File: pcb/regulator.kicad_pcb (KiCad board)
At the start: 2 copper layers, 60 x 68 mm, 28 parts, among them J1 Conn_01x06, U1 TL082

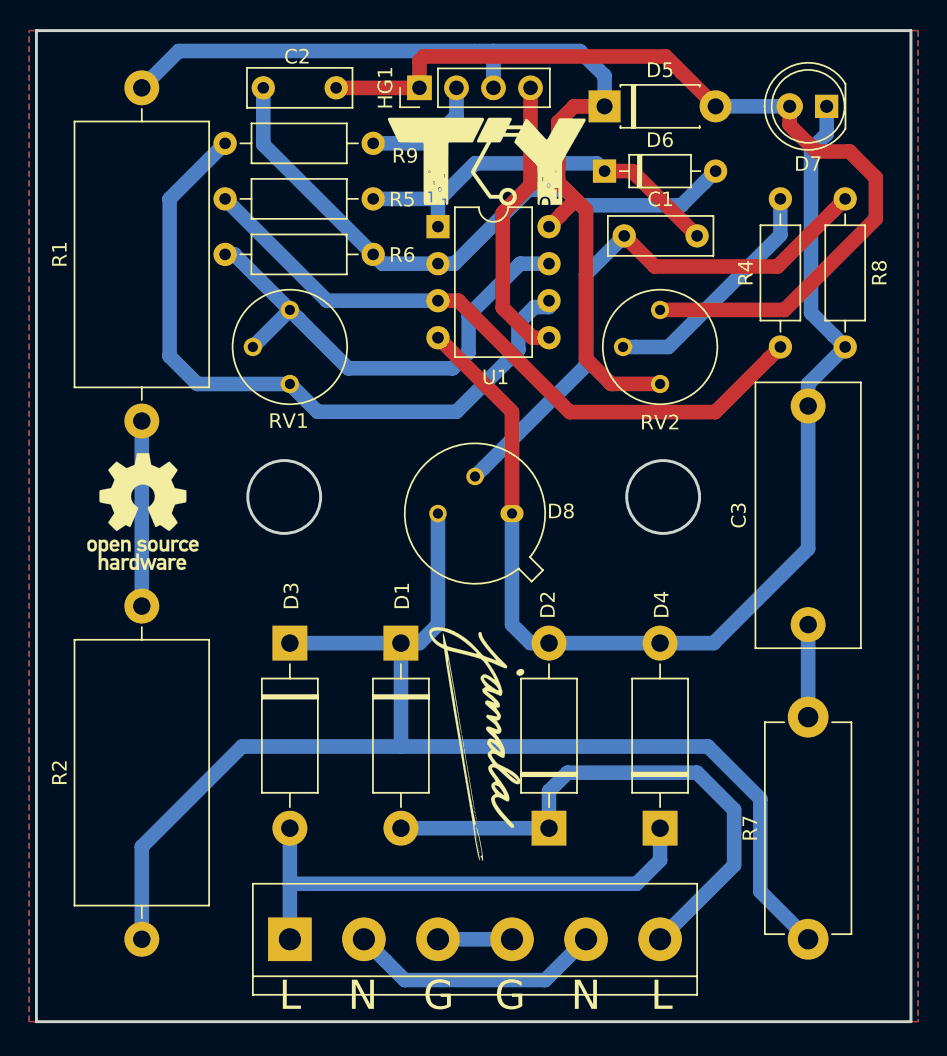
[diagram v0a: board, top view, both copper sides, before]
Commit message: Update QR code, exchange of mounting hole (add vias to outline)
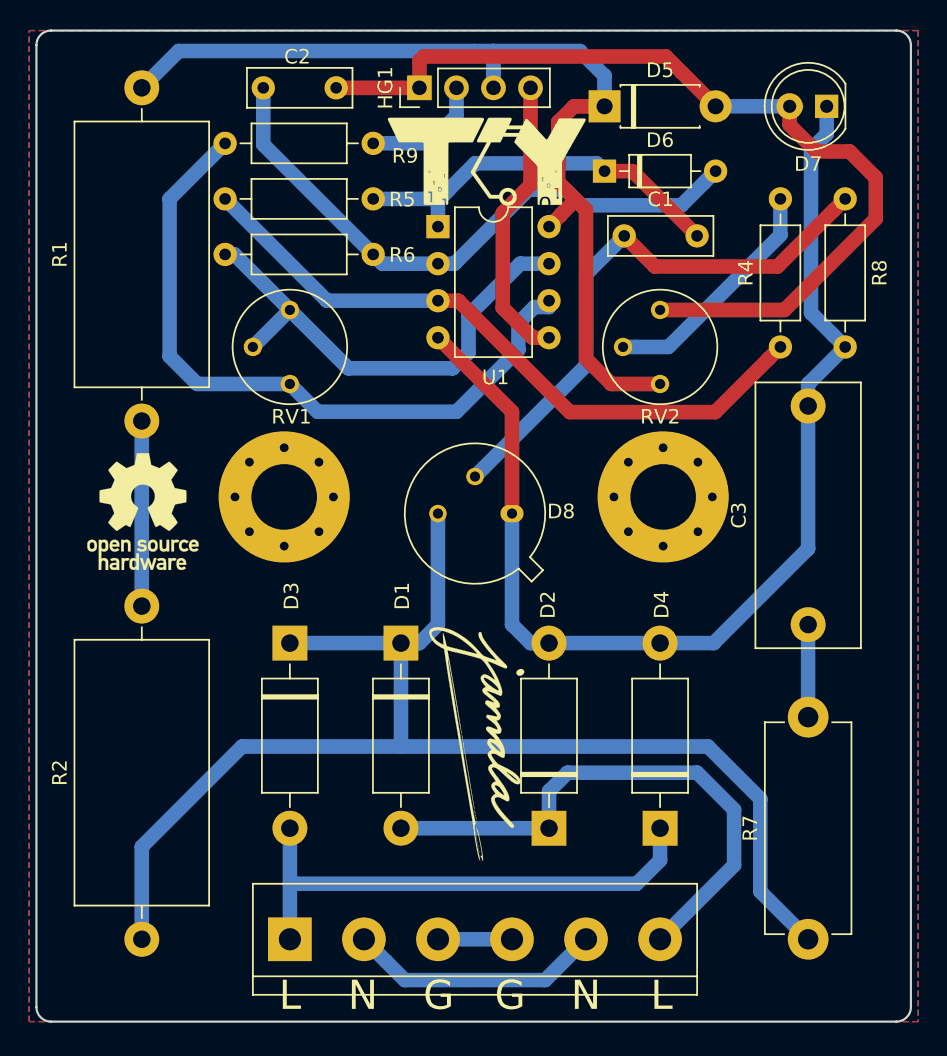
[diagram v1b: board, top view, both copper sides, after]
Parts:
- added REF**: MountingHole_4.5mm_Pad_Via, MountingHole:MountingHole_4.5mm_Pad_Via, F.Cu at (161.5, 103.0)
- added REF**: MountingHole_4.5mm_Pad_Via, MountingHole:MountingHole_4.5mm_Pad_Via, F.Cu at (135.5, 103.0)
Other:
- outline, holes or cut-outs redrawn
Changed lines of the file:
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@@
     (tracks 149)
     (zones 0)
-    (modules 28)
+    (modules 30)
     (nets 20)
   )
@@
     (visible_elements FFFFFF7F)
     (pcbplotparams
-      (layerselection 0x00000_ffffffff)
-      (usegerberextensions false)
+      (layerselection 0x010f0_ffffffff)
+      (usegerberextensions true)
       (usegerberattributes false)
       (usegerberadvancedattributes false)
@@
       (padsonsilk false)
       (subtractmaskfromsilk false)
-      (outputformat 4)
+      (outputformat 1)
       (mirror false)
-      (drillshape 2)
+      (drillshape 0)
       (scaleselection 1)
-      (outputdirectory ""))
+      (outputdirectory "gerber/"))
   )
   (net 0 "")
@@
     (descr "Potentiometer, vertical, Bourns 3339P, http://www.bourns.com/docs/Product-Datasheets/3339.pdf")
     (tags "Potentiometer vertical Bourns 3339P")
-    (fp_text reference RV1 (at -0.09 2.55) (layer F.SilkS)
+    (fp_text reference RV1 (at 0.11 2.25) (layer F.SilkS)
       (effects (font (size 1 1) (thickness 0.15)))
     )
@@
     (descr "Potentiometer, vertical, Bourns 3339P, http://www.bourns.com/docs/Product-Datasheets/3339.pdf")
     (tags "Potentiometer vertical Bourns 3339P")
-    (fp_text reference RV2 (at 0.01 2.65) (layer F.SilkS)
+    (fp_text reference RV2 (at 0.01 2.25) (layer F.SilkS)
       (effects (font (size 1 1) (thickness 0.15)))
     )
@@
       (xy 5.73024 -5.73024)) (layer B.SilkS) (width 0.01))
   )
+  (module MountingHole:MountingHole_4.5mm_Pad_Via (layer F.Cu)
+    (at 161.5 103)
+    (descr "Mounting Hole 4.5mm")
+    (tags "mounting hole 4.5mm")
+    (attr virtual)
+    (fp_text reference REF** (at 0 -5.5) (layer F.SilkS) hide
+      (effects (font (size 1 1) (thickness 0.15)))
+    )
+    (fp_text value MountingHole_4.5mm_Pad_Via (at 0 5.5) (layer F.Fab)
+      (effects (font (size 1 1) (thickness 0.15)))
+    )
+    (fp_circle (center 0 0) (end 4.75 0) (layer F.CrtYd) (width 0.05))
+    (fp_circle (center 0 0) (end 4.5 0) (layer Cmts.User) (width 0.15))
+    (fp_text user %R (at 0.3 0) (layer F.Fab)
+      (effects (font (size 1 1) (thickness 0.15)))
+    )
+    (pad 1 thru_hole circle (at 2.386485 -2.386485) (size 0.9 0.9) (drill 0.6) (layers *.Cu *.Mask))
+    (pad 1 thru_hole circle (at 0 -3.375) (size 0.9 0.9) (drill 0.6) (layers *.Cu *.Mask))
+    (pad 1 thru_hole circle (at -2.386485 -2.386485) (size 0.9 0.9) (drill 0.6) (layers *.Cu *.Mask))
+    (pad 1 thru_hole circle (at -3.375 0) (size 0.9 0.9) (drill 0.6) (layers *.Cu *.Mask))
+    (pad 1 thru_hole circle (at -2.386485 2.386485) (size 0.9 0.9) (drill 0.6) (layers *.Cu *.Mask))
+    (pad 1 thru_hole circle (at 0 3.375) (size 0.9 0.9) (drill 0.6) (layers *.Cu *.Mask))
+    (pad 1 thru_hole circle (at 2.386485 2.386485) (size 0.9 0.9) (drill 0.6) (layers *.Cu *.Mask))
+    (pad 1 thru_hole circle (at 3.375 0) (size 0.9 0.9) (drill 0.6) (layers *.Cu *.Mask))
+    (pad 1 thru_hole circle (at 0 0) (size 9 9) (drill 4.5) (layers *.Cu *.Mask))
+  )
+  (module MountingHole:MountingHole_4.5mm_Pad_Via (layer F.Cu)
+    (at 135.5 103)
+    (descr "Mounting Hole 4.5mm")
+    (tags "mounting hole 4.5mm")
+    (attr virtual)
+    (fp_text reference REF** (at 0 -5.5) (layer F.SilkS) hide
+      (effects (font (size 1 1) (thickness 0.15)))
+    )
+    (fp_text value MountingHole_4.5mm_Pad_Via (at 0 5.5) (layer F.Fab)
+      (effects (font (size 1 1) (thickness 0.15)))
+    )
+    (fp_circle (center 0 0) (end 4.75 0) (layer F.CrtYd) (width 0.05))
+    (fp_circle (center 0 0) (end 4.5 0) (layer Cmts.User) (width 0.15))
+    (fp_text user %R (at 0.3 0) (layer F.Fab)
+      (effects (font (size 1 1) (thickness 0.15)))
+    )
+    (pad 1 thru_hole circle (at 2.386485 -2.386485) (size 0.9 0.9) (drill 0.6) (layers *.Cu *.Mask))
+    (pad 1 thru_hole circle (at 0 -3.375) (size 0.9 0.9) (drill 0.6) (layers *.Cu *.Mask))
+    (pad 1 thru_hole circle (at -2.386485 -2.386485) (size 0.9 0.9) (drill 0.6) (layers *.Cu *.Mask))
+    (pad 1 thru_hole circle (at -3.375 0) (size 0.9 0.9) (drill 0.6) (layers *.Cu *.Mask))
+    (pad 1 thru_hole circle (at -2.386485 2.386485) (size 0.9 0.9) (drill 0.6) (layers *.Cu *.Mask))
+    (pad 1 thru_hole circle (at 0 3.375) (size 0.9 0.9) (drill 0.6) (layers *.Cu *.Mask))
+    (pad 1 thru_hole circle (at 2.386485 2.386485) (size 0.9 0.9) (drill 0.6) (layers *.Cu *.Mask))
+    (pad 1 thru_hole circle (at 3.375 0) (size 0.9 0.9) (drill 0.6) (layers *.Cu *.Mask))
+    (pad 1 thru_hole circle (at 0 0) (size 9 9) (drill 4.5) (layers *.Cu *.Mask))
+  )
+  (gr_line (start 177.5 139) (end 119.5 139) (layer Edge.Cuts) (width 0.15))
+  (gr_arc (start 177.5 138) (end 177.5 139) (angle -90) (layer Edge.Cuts) (width 0.15))
+  (gr_arc (start 119.5 138) (end 118.5 138) (angle -90) (layer Edge.Cuts) (width 0.15))
+  (gr_line (start 118.5 72) (end 118.5 138) (layer Edge.Cuts) (width 0.15))
+  (gr_line (start 178.5 72) (end 178.5 138) (layer Edge.Cuts) (width 0.15))
+  (gr_line (start 119.5 71) (end 177.5 71) (layer Edge.Cuts) (width 0.15))
+  (gr_arc (start 119.5 72) (end 119.5 71) (angle -90) (layer Edge.Cuts) (width 0.15))
+  (gr_arc (start 177.5 72) (end 178.5 72) (angle -90) (layer Edge.Cuts) (width 0.15))
   (gr_text L (at 161.4 137.2) (layer F.SilkS)
     (effects (font (size 2 2) (thickness 0.4)))
@@
   )
   (gr_line (start 148.59 70.485) (end 148.59 67.945) (layer Cmts.User) (width 0.2))
-  (gr_circle (center 135.5 103.08) (end 130.48 102.65) (layer Cmts.User) (width 0.2))
-  (gr_circle (center 161.49 103.08) (end 156.47 102.71) (layer Cmts.User) (width 0.2))
-  (gr_circle (center 135.5011 103.0036) (end 138.0011 103.0036) (layer Edge.Cuts) (width 0.2))
-  (gr_line (start 178.5011 71.0036) (end 118.5011 71.0036) (layer Edge.Cuts) (width 0.2))
-  (gr_line (start 178.5011 71.0036) (end 178.5011 139.0036) (layer Edge.Cuts) (width 0.2))
-  (gr_circle (center 161.5011 103.0036) (end 164.0011 103.0036) (layer Edge.Cuts) (width 0.2))
-  (gr_line (start 118.5011 71.0036) (end 118.5011 139.0036) (layer Edge.Cuts) (width 0.2))
-  (gr_line (start 178.5011 139.0036) (end 118.5011 139.0036) (layer Edge.Cuts) (width 0.2))
   (segment (start 149.189999 101.000001) (end 148.59 101.6) (width 1) (layer B.Cu) (net 1) (status 30))
   (segment (start 158.83 85.09) (end 156.21 87.71) (width 1) (layer B.Cu) (net 1) (status 10))
@@
   (segment (start 129.54 95.25) (end 135.89 95.25) (width 1) (layer B.Cu) (net 18) (status 20))
   (segment (start 127.635 93.345) (end 129.54 95.25) (width 1) (layer B.Cu) (net 18))
+  (segment (start 152.661999 89.974999) (end 153.67 89.974999) (width 1) (layer B.Cu) (net 18) (status 20))
+  (segment (start 151.569999 91.066999) (end 152.661999 89.974999) (width 1) (layer B.Cu) (net 18))
+  (segment (start 151.569999 92.905001) (end 151.569999 91.066999) (width 1) (layer B.Cu) (net 18))
+  (segment (start 147.32 97.155) (end 151.569999 92.905001) (width 1) (layer B.Cu) (net 18))
+  (segment (start 135.89 95.25) (end 137.795 97.155) (width 1) (layer B.Cu) (net 18) (status 10))
+  (segment (start 137.795 97.155) (end 147.32 97.155) (width 1) (layer B.Cu) (net 18))
   (segment (start 153.67 89.974999) (end 153.67 89.535) (width 1) (layer B.Cu) (net 18) (status 30))
-  (segment (start 137.795 97.155) (end 147.32 97.155) (width 1) (layer B.Cu) (net 18))
-  (segment (start 152.661999 89.974999) (end 153.67 89.974999) (width 1) (layer B.Cu) (net 18) (status 20))
-  (segment (start 135.89 95.25) (end 137.795 97.155) (width 1) (layer B.Cu) (net 18) (status 10))
-  (segment (start 147.32 97.155) (end 151.569999 92.905001) (width 1) (layer B.Cu) (net 18))
-  (segment (start 151.569999 92.905001) (end 151.569999 91.066999) (width 1) (layer B.Cu) (net 18))
-  (segment (start 151.569999 91.066999) (end 152.661999 89.974999) (width 1) (layer B.Cu) (net 18))
   (segment (start 165.1 76.2) (end 170.18 76.2) (width 1) (layer B.Cu) (net 19))
   (segment (start 144.78 74.93) (end 139.065 74.93) (width 1) (layer F.Cu) (net 19))
